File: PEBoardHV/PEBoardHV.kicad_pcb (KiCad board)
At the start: 2 copper layers, 106.7 x 76.2 mm, 54 parts, among them J1 To PE LV, J10 Discharge Jumper, J2 Left Connector (Master), J3 E-Meter Internal, J4 Right Connector (Slave), J5 E-Meter External, J6 HV Cable, J7 TSMPs, J8 HV CAN Debug, J9 EMeter HV, U1 L78S05CV-DG, U2 ISO1050, U3 PS2501-4, U4 DK1A1B-12V, U5 DK1A1B-12V

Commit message: tweak boards slightly
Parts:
- C1, C2, C3: footprint Capacitors_THT:CP_Radial_D5.0mm_P2.50mm -> Capacitors_THT:C_Disc_D3.0mm_W1.6mm_P2.50mm
- moved R1 10.2 mm to (162.3, 64.0), turned to 90 degrees
- moved C3 3.31 mm to (125.5, 61.5)
- moved D1 1.27 mm to (154.7, 55.1), turned to 180 degrees
- moved C2 0.80 mm to (128.0, 84.3)
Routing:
- net /TS+_SWITCHED_L: track 0.00 -> 147.0 mm
- net /TS+_SWITCHED_R: track 0.00 -> 108.5 mm
- net /TS+: track 0.00 -> 91.6 mm
- net /5V_TS: track 0.00 -> 72.3 mm
- net /TS-: track 0.00 -> 59.3 mm, vias 0 -> 4
- net /AIRS_FINAL: track 0.00 -> 54.3 mm
- net /TS+_FUSED: track 0.00 -> 51.8 mm
- net Net-(R8-Pad2): track 0.00 -> 46.7 mm
- net Net-(R4-Pad2): track 0.00 -> 46.7 mm
- net Net-(R2-Pad2): track 0.00 -> 46.7 mm
- net +12V: track 0.00 -> 42.5 mm
- net Net-(D2-Pad1): track 0.00 -> 41.7 mm
- net Net-(D4-Pad1): track 0.00 -> 41.5 mm
- net /CAN+: track 0.00 -> 37.9 mm
- net /CAN_L_BOARD: track 0.00 -> 35.9 mm
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
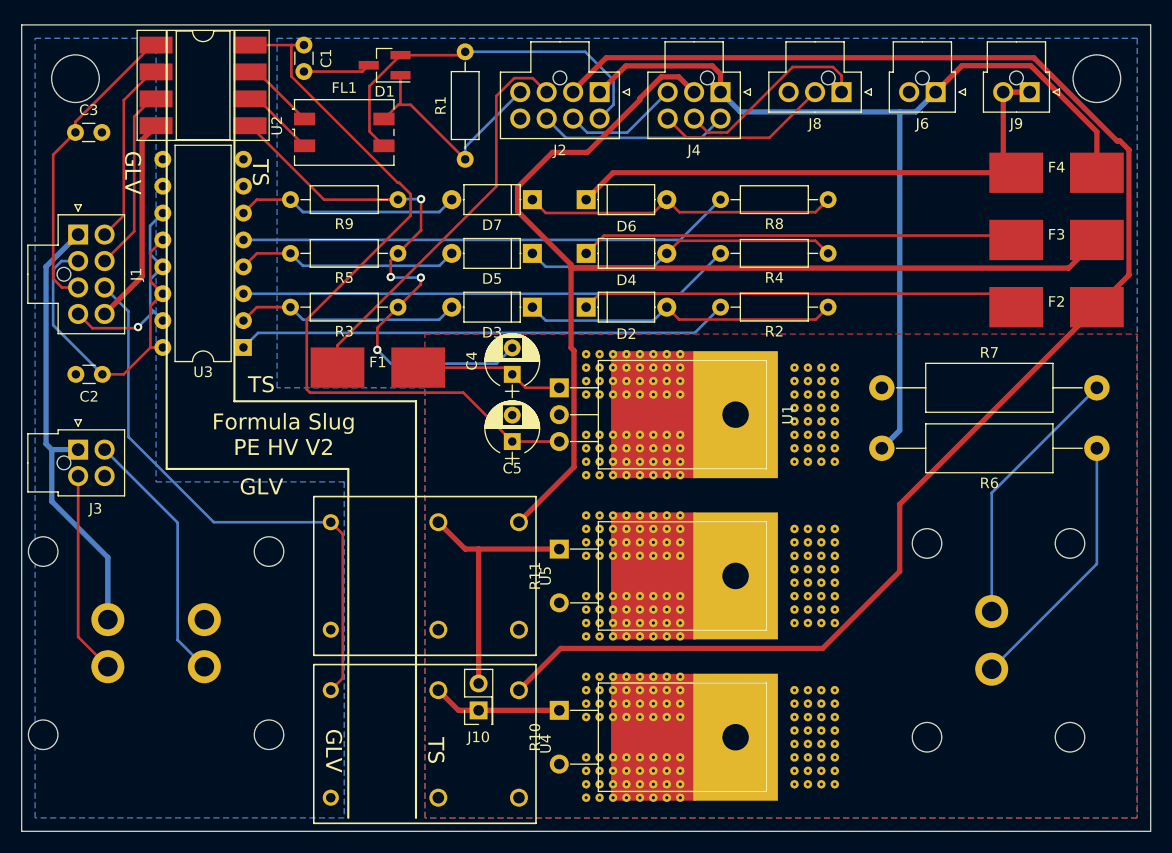
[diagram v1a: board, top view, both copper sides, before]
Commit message: add diodes to relay coils among other things
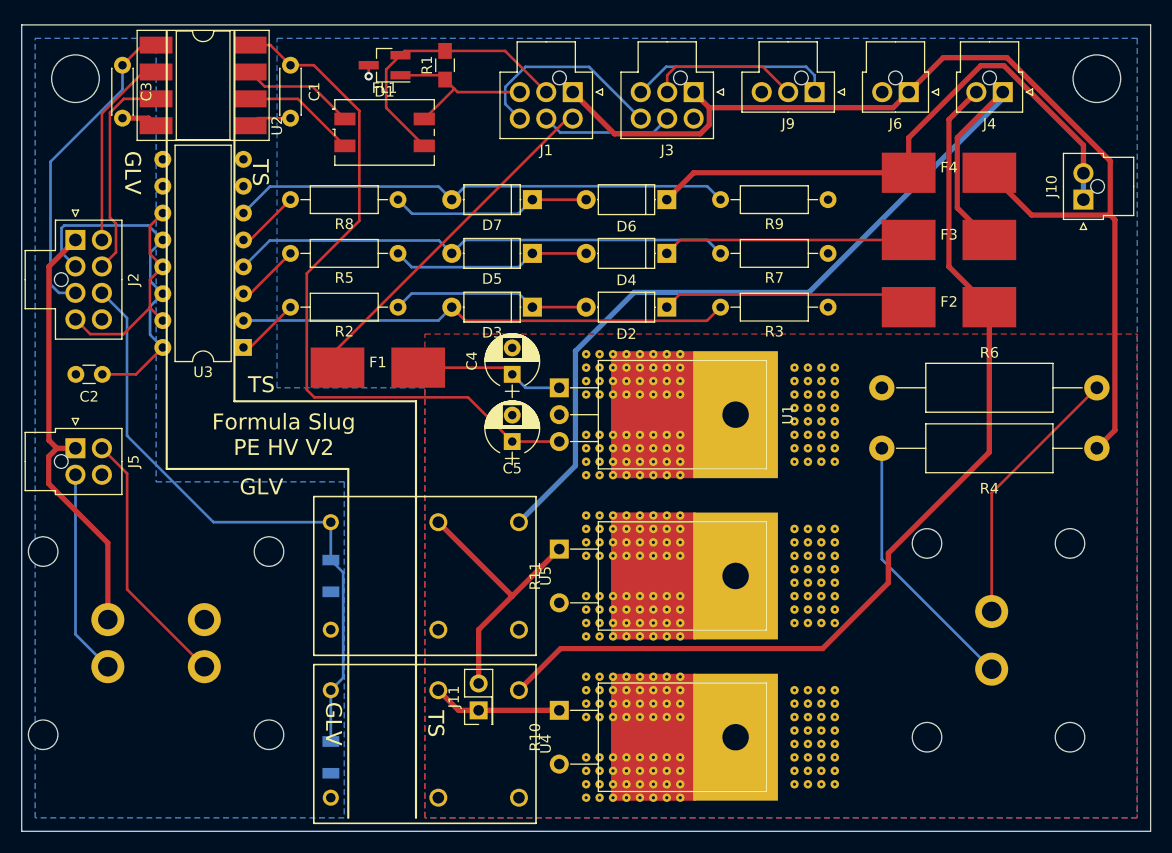
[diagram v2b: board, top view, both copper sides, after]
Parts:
- added D8: D, Diodes_SMD:D_1206, B.Cu at (149.6, 103.4)
- added D9: D, Diodes_SMD:D_1206, B.Cu at (149.6, 120.5)
- added J11: Discharge Jumper, Pin_Headers:Pin_Header_Straight_2x01_Pitch2.54mm, F.Cu at (163.6, 116.1)
- C1, C3: footprint Capacitors_THT:C_Disc_D3.0mm_W1.6mm_P2.50mm -> Capacitors_THT:C_Disc_D4.3mm_W1.9mm_P5.00mm
- J1: value To PE LV -> Left Connector (Master); footprint Connectors_Molex:Molex_NanoFit_2x04x2.50mm_Straight -> Connectors_Molex:Molex_NanoFit_2x03x2.50mm_Straight
- J10: value Discharge Jumper -> EMeter HV; footprint Pin_Headers:Pin_Header_Straight_2x01_Pitch2.54mm -> Connectors_Molex:Molex_NanoFit_1x02x2.50mm_Straight
- J2: value Left Connector (Master) -> To PE LV
- J3: value E-Meter Internal -> Right Connector (Slave); footprint Connectors_Molex:Molex_NanoFit_2x02x2.50mm_Straight -> Connectors_Molex:Molex_NanoFit_2x03x2.50mm_Straight
- J4: value Right Connector (Slave) -> Ring Terminal Connector; footprint Connectors_Molex:Molex_NanoFit_2x03x2.50mm_Straight -> Connectors_Molex:Molex_NanoFit_1x02x2.50mm_Straight
- J5: value E-Meter External -> E-Meter Internal; footprint FSFootprints:DT15-4P -> Connectors_Molex:Molex_NanoFit_2x02x2.50mm_Straight; moved to F.Cu
- J7: value TSMPs -> E-Meter External; footprint FSFootprints:DT15-2P -> FSFootprints:DT15-4P
- J8: value HV CAN Debug -> TSMPs; footprint Connectors_Molex:Molex_NanoFit_1x03x2.50mm_Straight -> FSFootprints:DT15-2P; moved to B.Cu
- J9: value EMeter HV -> HV CAN Debug; footprint Connectors_Molex:Molex_NanoFit_1x02x2.50mm_Straight -> Connectors_Molex:Molex_NanoFit_1x03x2.50mm_Straight
- R1: footprint Resistors_THT:R_Axial_DIN0207_L6.3mm_D2.5mm_P10.16mm_Horizontal -> Resistors_SMD:R_0805_HandSoldering
- R4: value 1.2kR -> 5kR; footprint Resistors_THT:R_Axial_DIN0207_L6.3mm_D2.5mm_P10.16mm_Horizontal -> Resistors_THT:R_Axial_DIN0414_L11.9mm_D4.5mm_P20.32mm_Horizontal
- R5: value 1.5k -> 1.2kR
- R7: value 5kR -> 1.5k; footprint Resistors_THT:R_Axial_DIN0414_L11.9mm_D4.5mm_P20.32mm_Horizontal -> Resistors_THT:R_Axial_DIN0207_L6.3mm_D2.5mm_P10.16mm_Horizontal
- moved J7 86.8 mm to (133.1, 109.7), turned to 0 degrees
- moved J10 74.8 mm to (220.7, 67.8)
- moved J3 67.3 mm to (183.9, 57.7), turned to 180 degrees
- moved J8 64.7 mm to (219.5, 118.6)
- moved J2 51.5 mm to (125.5, 71.6), turned to 270 degrees
- moved J1 48.6 mm to (172.5, 57.7), turned to 180 degrees
- moved R2 40.6 mm to (156.0, 78.0)
- moved R3 40.6 mm to (196.6, 78.0)
- moved R8 40.6 mm to (156.0, 67.8)
- moved R9 40.6 mm to (196.6, 67.8)
- moved J4 26.7 mm to (213.1, 57.7)
- moved R6 21.1 mm to (201.7, 85.6), turned to 0 degrees
- moved J9 20.3 mm to (195.3, 57.7)
- moved J5 19.9 mm to (125.5, 91.3), turned to 270 degrees
- moved R4 19.1 mm to (201.7, 91.3), turned to 0 degrees
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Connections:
- J1 pad 1: +12V -> /TS+
- J1 pad 2: /5V_GLV -> /CAN_L_BOARD
- J1 pad 3: /3.3V_GLV -> /CAN_H_BOARD
- J1 pad 4: /SIG_TSAL -> /CAN+
- J1 pad 5: /CAN_RX -> /CAN_L_CONTROLLER
- J1 pad 6: /CAN_TX -> /CAN_H_CONTROLLER
- J10 pad 1: /DISCHARGE_L -> /TS+_FUSED
- J10 pad 2: /DISCHARGE_R -> /TS+_FUSED
- J2 pad 1: /TS+ -> +12V
- J2 pad 2: /TS+_SWITCHED_L -> /5V_GLV
- J2 pad 3: /CAN+ -> /3.3V_GLV
- J2 pad 4: /CAN_H_BOARD -> /SIG_TSAL
- J2 pad 5: /CAN_L_BOARD -> /CAN_RX
- J2 pad 6: /CAN_H_CONTROLLER -> /CAN_TX
- J2 pad 7: /CAN_L_CONTROLLER -> /AIRS_FINAL
- J2 pad 8: (no net) -> GND
- J3 pad 1: +12V -> /TS+
- J3 pad 2: /EM_SIG+ -> /CAN_L_DEBUG
- J3 pad 3: /EM_SIG- -> /CAN_H_DEBUG
- J3 pad 4: GND -> (no net)
- J4 pad 1: /TS+ -> /TS+_SWITCHED_R
- J4 pad 2: /TS+_SWITCHED_R -> /TS+_SWITCHED_L
- J7 pad 1: Net-(J7-Pad1) -> +12V
- J7 pad 2: Net-(J7-Pad2) -> /EM_SIG+
- J8 pad 1: /CAN_H_DEBUG -> Net-(J8-Pad1)
- J8 pad 2: /CAN_L_DEBUG -> Net-(J8-Pad2)
- J9 pad 1: /TS+_FUSED -> /CAN_H_DEBUG
- J9 pad 2: /TS+_FUSED -> /CAN_L_DEBUG
- R4 pad 1: Net-(D4-Pad2) -> Net-(J8-Pad1)
- R4 pad 2: Net-(R4-Pad2) -> /TS+
- R5 pad 1: /TS- -> Net-(D4-Pad2)
- R5 pad 2: Net-(D5-Pad2) -> Net-(R5-Pad2)
- R6 pad 1: Net-(J7-Pad1) -> /TS-
- R6 pad 2: /TS+ -> Net-(J8-Pad2)
- R7 pad 2: Net-(J7-Pad2) -> Net-(D5-Pad2)
- U3 pad 3: Net-(R4-Pad2) -> Net-(R5-Pad2)
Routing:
- net /TS+_SWITCHED_L: track 147.0 -> 92.1 mm
- net /TS-: track 59.3 -> 5.15 mm, vias 4 -> 1
- net Net-(R4-Pad2): track 46.7 -> 0.00 mm
- net Net-(R8-Pad2): track 46.7 -> 6.02 mm
- net Net-(R2-Pad2): track 46.7 -> 6.02 mm
- net Net-(D7-Pad2): track 21.2 -> 47.7 mm
- net Net-(D5-Pad2): track 21.2 -> 47.7 mm
- net Net-(D3-Pad2): track 21.2 -> 46.7 mm
- net Net-(J8-Pad2): track 0.00 -> 25.3 mm
- net Net-(J7-Pad2): track 25.3 -> 0.00 mm
- net Net-(J8-Pad1): track 0.00 -> 25.2 mm
- net Net-(J7-Pad1): track 25.0 -> 0.00 mm
- net /TS+_SWITCHED_R: track 108.5 -> 86.3 mm
- net Net-(D4-Pad1): track 41.5 -> 23.4 mm
- net Net-(D2-Pad1): track 41.7 -> 23.8 mm
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
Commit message: Update 60V circuit some more, on both boards
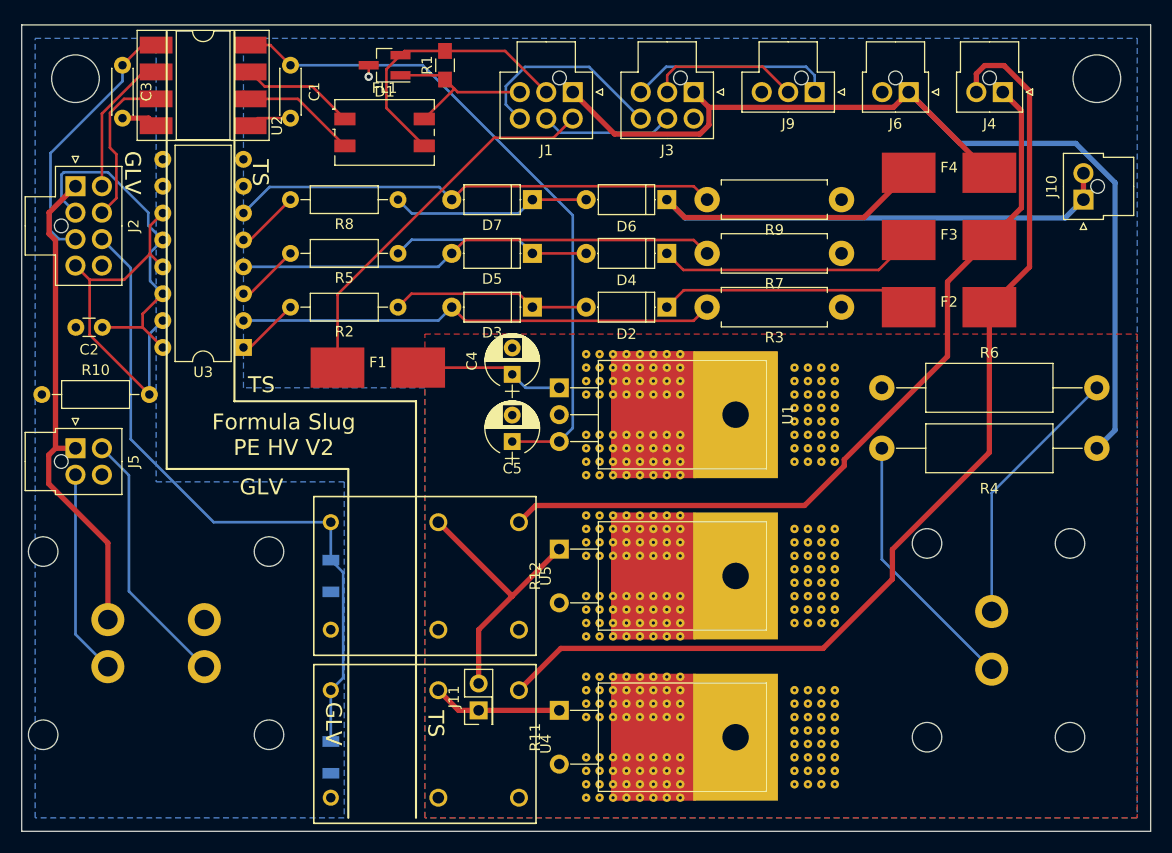
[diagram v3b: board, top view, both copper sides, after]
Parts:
- added R12: 1K, FSFootprints:TO-220-2_Horizontal_HeatSunk, F.Cu at (171.2, 100.8)
- R10: value 1K -> 100k; footprint FSFootprints:TO-220-2_Horizontal_HeatSunk -> Resistors_THT:R_Axial_DIN0207_L6.3mm_D2.5mm_P10.16mm_Horizontal
- R2, R5, R8: value 1.2kR -> 1.2k
- R3, R7, R9: value 1.5k -> 10k; footprint Resistors_THT:R_Axial_DIN0207_L6.3mm_D2.5mm_P10.16mm_Horizontal -> Resistors_THT:R_Axial_DIN0411_L9.9mm_D3.6mm_P12.70mm_Horizontal
- moved R10 57.3 mm to (122.3, 86.2), turned to 0 degrees
- moved R11 15.2 mm to (171.2, 116.1)
- moved J2 5.08 mm to (125.5, 66.5)
- moved C2 4.45 mm to (128.0, 79.9)
- moved R3 1.27 mm to (197.9, 78.0)
- moved R7 1.27 mm to (197.9, 72.9)
- moved R9 1.27 mm to (197.9, 67.8)
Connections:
- R10 pad 1: /DISCHARGE_L -> GND
- R10 pad 2: /TS- -> /SIG_TSAL
- R11 pad 1: /DISCHARGE_R -> /DISCHARGE_L
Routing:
- net /SIG_TSAL: track 20.8 -> 35.4 mm
- net /TS+_FUSED: track 54.8 -> 68.6 mm
- net /TS+_SWITCHED_R: track 86.3 -> 75.9 mm
- net /TS+_SWITCHED_L: track 92.1 -> 99.2 mm
- net /TS+: track 103.6 -> 97.7 mm
- net +12V: track 41.6 -> 46.7 mm
- net /CAN_RX: track 18.7 -> 13.6 mm
- net /3.3V_GLV: track 30.2 -> 25.1 mm
- net /AIRS_FINAL: track 58.8 -> 63.9 mm
- net /CAN_TX: track 20.2 -> 15.2 mm
- net /5V_TS: track 67.2 -> 63.5 mm
- net /CAN+: track 33.0 -> 36.0 mm
- net Net-(D5-Pad2): track 47.7 -> 45.4 mm
- net Net-(D7-Pad2): track 47.7 -> 46.4 mm
- net Net-(D4-Pad1): track 23.4 -> 24.7 mm
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
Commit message: hopefully finalize PCBs for send to manufacturing
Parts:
- moved D9 1.27 mm to (149.6, 119.3)
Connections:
- net Net-(D2-Pad1) renamed /TS+_LF
- net Net-(D4-Pad1) renamed /TS+_RF
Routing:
- net /TS+_SWITCHED_R: track 75.9 -> 92.2 mm
- net /TS+: track 97.7 -> 82.4 mm, vias 0 -> 1
- net /TS+_FUSED: track 68.6 -> 55.5 mm
- net /TS+_SWITCHED_L: track 99.2 -> 90.9 mm
- net /5V_TS: track 63.5 -> 67.2 mm
- net /AIRS_FINAL: track 63.9 -> 62.6 mm
- net /TS+_RF: track 24.7 -> 24.0 mm
- net Net-(D3-Pad2): track 45.4 -> 45.9 mm
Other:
- net class HV added: clearance 0.6, trace_width 0.25, via_dia 0.8, via_drill 0.4
- net class TSPower added: clearance 0.6, trace_width 0.25, via_dia 0.8, via_drill 0.4

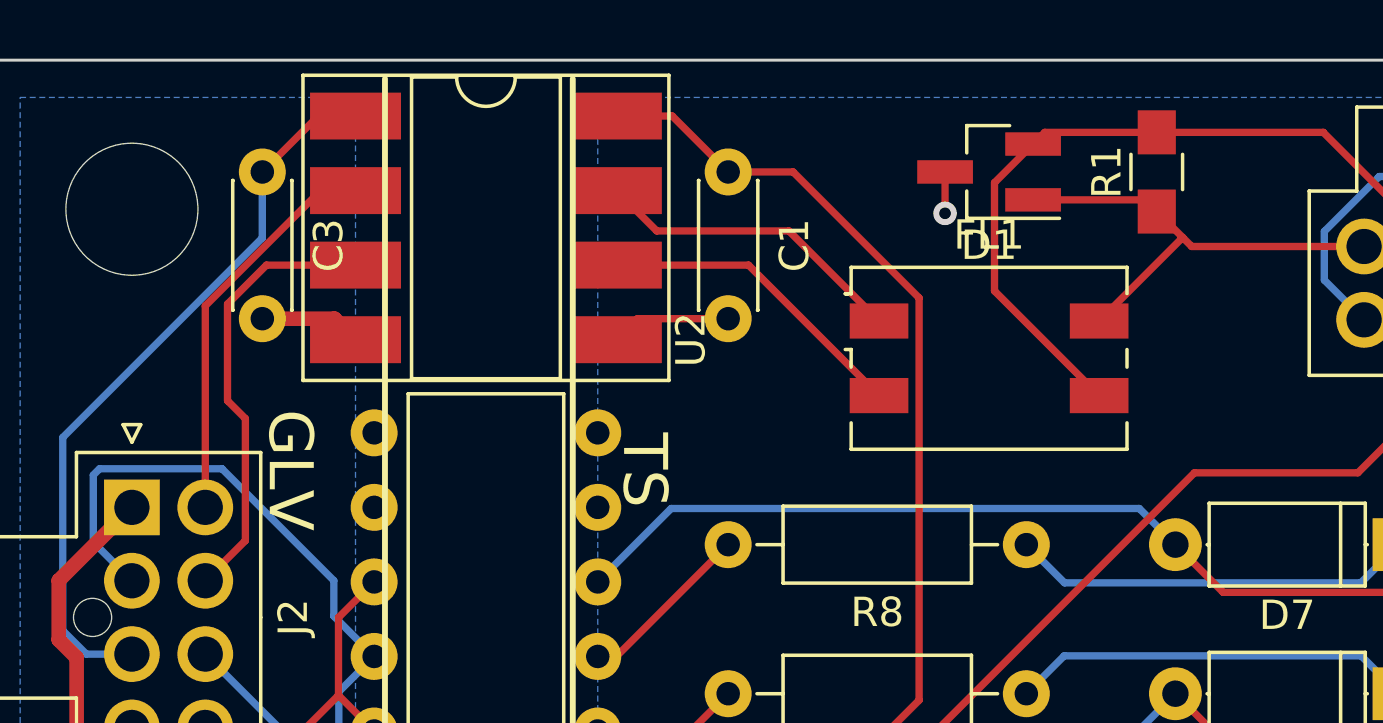
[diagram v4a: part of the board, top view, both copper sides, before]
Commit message: Edit some component labels and other items for PCB send out
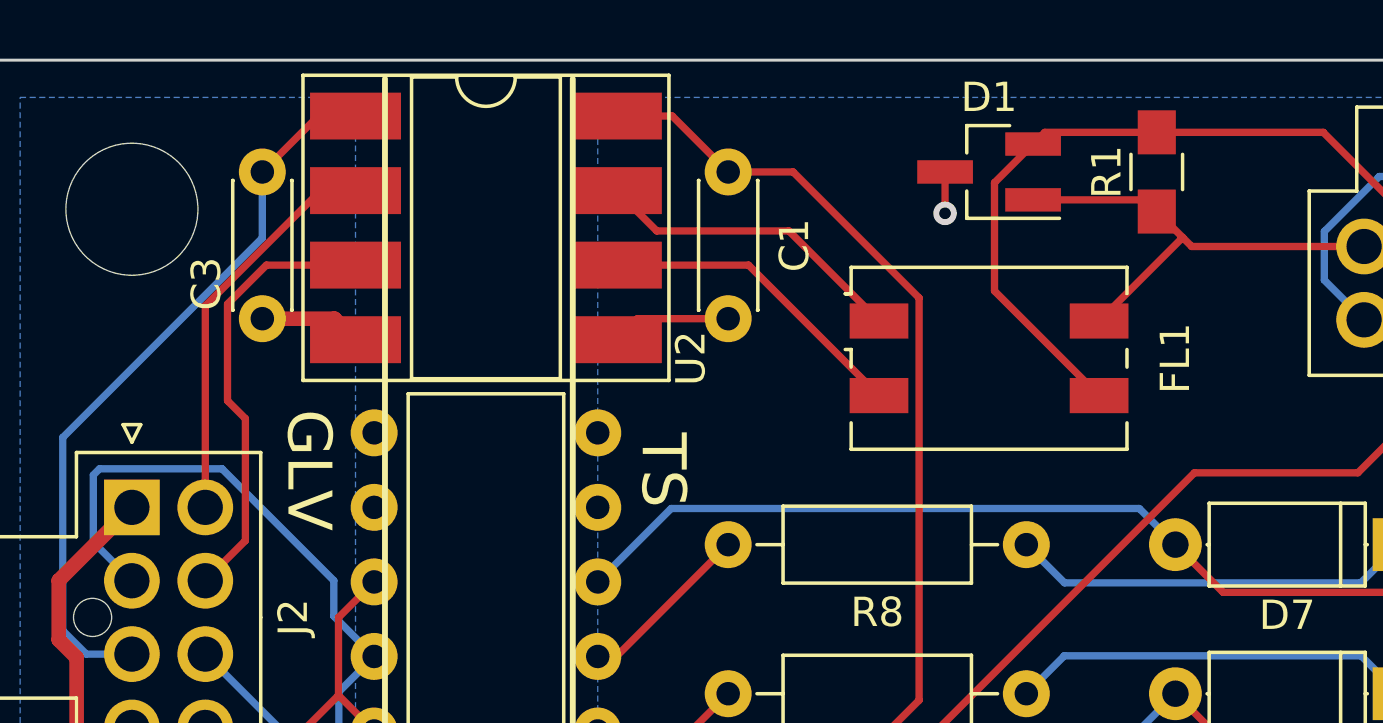
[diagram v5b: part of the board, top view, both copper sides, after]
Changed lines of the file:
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@@
     (links 389)
     (no_connects 0)
-    (area 120.345999 51.257999 227.126001 127.558001)
+    (area 114.795999 49.513 228.971 130.253)
     (thickness 1.6)
     (drawings 23)
@@
     (tags "THT DIP DIL PDIP 2.54mm 8.89mm 350mil SMDSocket LongPads")
     (attr smd)
-    (fp_text reference U2 (at 6.985 3.81 90) (layer F.SilkS)
+    (fp_text reference U2 (at 6.985 4.445 90) (layer F.SilkS)
       (effects (font (size 1 1) (thickness 0.15)))
     )
@@
     (tags SOT-23)
     (attr smd)
-    (fp_text reference D1 (at 0 -2.5 180) (layer F.SilkS)
+    (fp_text reference D1 (at 0 2.54 180) (layer F.SilkS)
       (effects (font (size 1 1) (thickness 0.15)))
     )
@@
     (tags "Wuerth WE-SL2")
     (attr smd)
-    (fp_text reference FL1 (at 0 -4.2) (layer F.SilkS)
+    (fp_text reference FL1 (at 6.35 0 90) (layer F.SilkS)
       (effects (font (size 1 1) (thickness 0.15)))
     )
@@
     (descr "C, Disc series, Radial, pin pitch=5.00mm, , diameter*width=4.3*1.9mm^2, Capacitor, http://www.vishay.com/docs/45233/krseries.pdf")
     (tags "C Disc series Radial pin pitch 5.00mm  diameter 4.3mm width 1.9mm Capacitor")
-    (fp_text reference C3 (at 2.5 -2.26 270) (layer F.SilkS)
+    (fp_text reference C3 (at 3.81 1.905 270) (layer F.SilkS)
       (effects (font (size 1 1) (thickness 0.15)))
     )
@@
     (effects (font (size 1.5 1.5) (thickness 0.3)) (justify mirror))
   )
-  (gr_text "TS\n\n\n\n\nGLV" (at 136.906 65.278 270) (layer B.SilkS)
+  (gr_text "TS\n\n\n\n\nGLV" (at 137.541 65.278 270) (layer B.SilkS)
     (effects (font (size 1.5 1.5) (thickness 0.3)) (justify mirror))
   )
-  (gr_text "TS\n\n\n\n\nGLV" (at 136.906 65.278 270) (layer F.SilkS)
+  (gr_text "TS\n\n\n\n\nGLV" (at 137.541 65.278 270) (layer F.SilkS)
     (effects (font (size 1.5 1.5) (thickness 0.3)))
   )
